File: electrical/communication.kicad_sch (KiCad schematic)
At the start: 23 parts

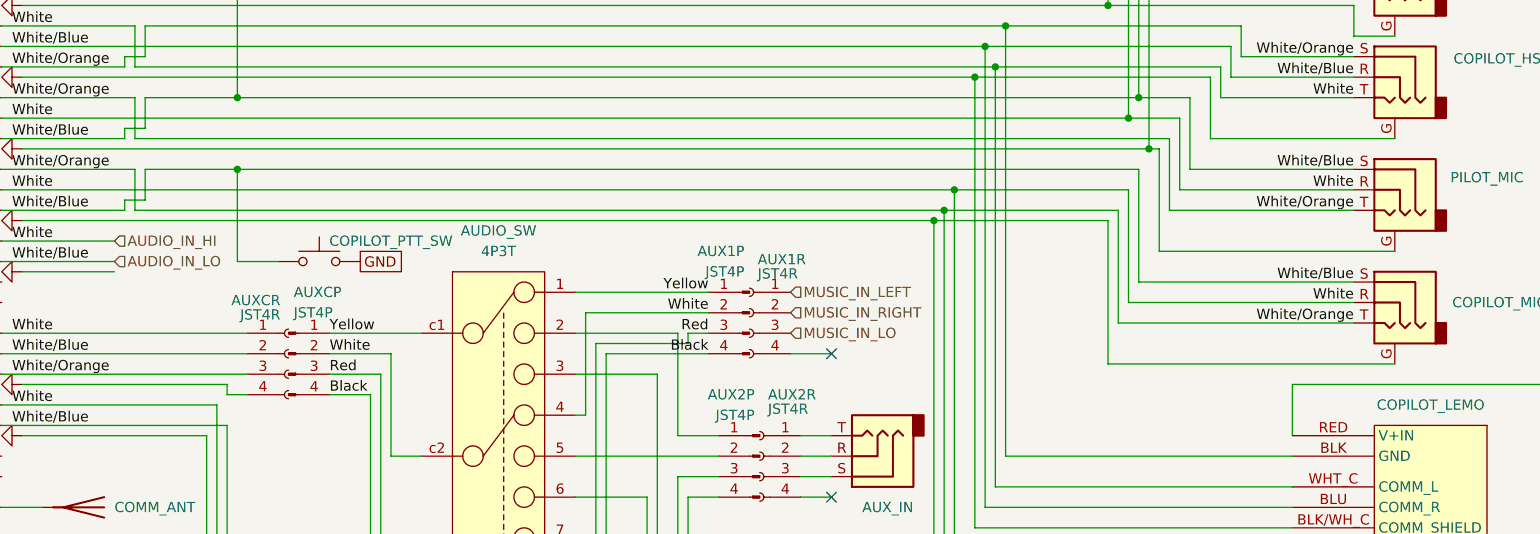
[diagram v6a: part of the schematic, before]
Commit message: Changed comms PTT and removed shield to TRS plugs. Fixed backwards GDU TX/RX wiring for GSU.
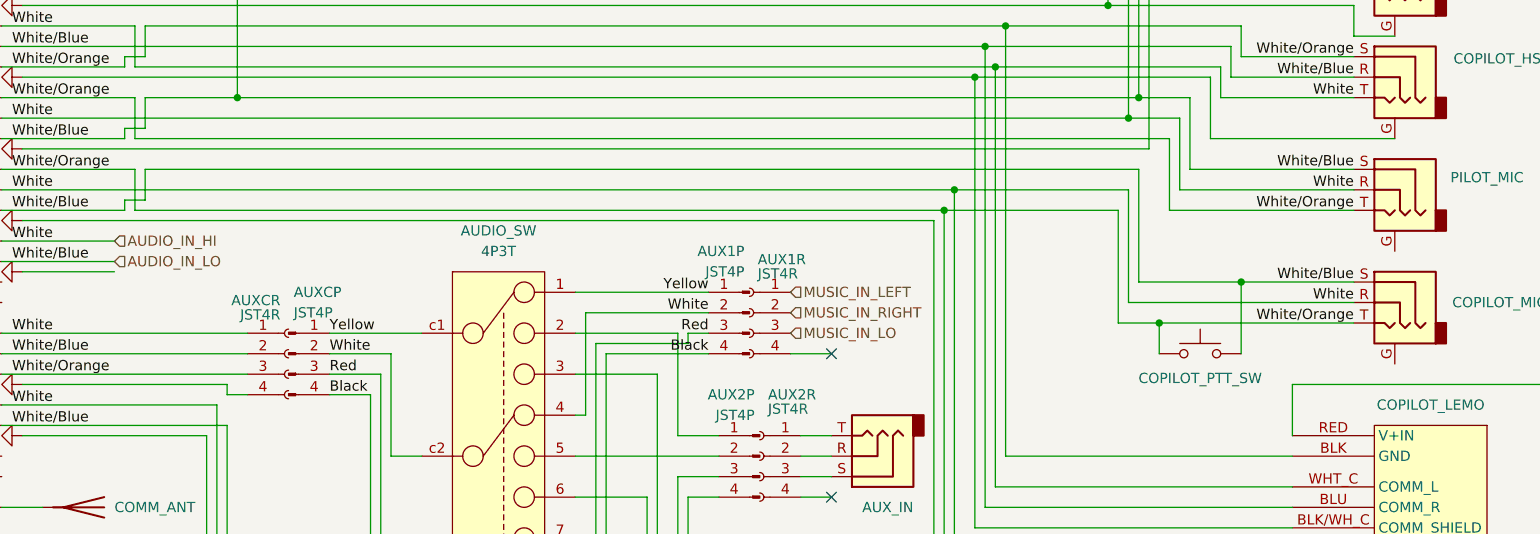
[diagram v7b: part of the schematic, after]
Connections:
- net AUDIO_IN_LO: now also COPILOT_PTT_SW.2; no longer COPILOT_PTT_SW.1
- net GND: no longer COPILOT_PTT_SW.2
- net GNDS: no longer COPILOT_MIC.G, PILOT_MIC.G
- net White/Orange: now also COPILOT_PTT_SW.1
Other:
- moved on the sheet: COPILOT_PTT_SW
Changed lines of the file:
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@@
 	(title_block
 		(title "Communication")
-		(date "2026-01-06")
-		(rev "1.2.5")
+		(date "2026-01-08")
+		(rev "1.2.6")
 		(company "N877RV")
 	)
@@
 	)
 	(junction
-		(at 180.34 87.63)
-		(diameter 0)
-		(color 0 0 0 0)
-	)
-	(junction
 		(at 76.2 34.29)
 		(diameter 0)
@@
 	)
 	(junction
-		(at 93.98 81.28)
-		(diameter 0)
-		(color 0 0 0 0)
-	)
-	(junction
 		(at 205.74 72.39)
 		(diameter 0)
@@
 	)
 	(junction
-		(at 198.12 54.61)
+		(at 208.28 100.33)
 		(diameter 0)
 		(color 0 0 0 0)
 	)
 	(junction
-		(at 207.01 78.74)
+		(at 198.12 54.61)
 		(diameter 0)
 		(color 0 0 0 0)
@@
 	)
 	(junction
+		(at 218.44 95.25)
+		(diameter 0)
+		(color 0 0 0 0)
+	)
+	(junction
 		(at 224.79 22.86)
 		(diameter 0)
@@
 	(wire
 		(pts
-			(xy 207.01 78.74) (xy 208.28 78.74)
-		)
-		(stroke
-			(width 0)
-			(type dash)
-		)
-	)
-	(wire
-		(pts
 			(xy 91.44 110.49) (xy 91.44 137.16)
 		)
@@
 	(wire
 		(pts
-			(xy 208.28 91.44) (xy 237.49 91.44)
-		)
-		(stroke
-			(width 0)
-			(type dash)
-		)
-	)
-	(wire
-		(pts
 			(xy 149.86 121.92) (xy 149.86 147.32)
 		)
@@
 	(wire
 		(pts
-			(xy 99.06 92.71) (xy 93.98 92.71)
-		)
-		(stroke
-			(width 0)
-			(type default)
-		)
-	)
-	(wire
-		(pts
 			(xy 81.28 63.5) (xy 81.28 68.58)
 		)
@@
 	(wire
 		(pts
-			(xy 201.93 105.41) (xy 237.49 105.41)
-		)
-		(stroke
-			(width 0)
-			(type dash)
-		)
-	)
-	(wire
-		(pts
 			(xy 224.79 107.95) (xy 256.54 107.95)
 		)
@@
 	(wire
 		(pts
-			(xy 180.34 87.63) (xy 201.93 87.63)
-		)
-		(stroke
-			(width 0)
-			(type dash)
-		)
-	)
-	(wire
-		(pts
 			(xy 232.41 59.69) (xy 199.39 59.69)
 		)
@@
 	(wire
 		(pts
+			(xy 218.44 95.25) (xy 205.74 95.25)
+		)
+		(stroke
+			(width 0)
+			(type default)
+		)
+	)
+	(wire
+		(pts
 			(xy 189.23 63.5) (xy 218.44 63.5)
 		)
@@
 	(wire
 		(pts
-			(xy 232.41 95.25) (xy 205.74 95.25)
+			(xy 232.41 95.25) (xy 218.44 95.25)
 		)
 		(stroke
@@
 	(wire
 		(pts
-			(xy 208.28 78.74) (xy 208.28 91.44)
-		)
-		(stroke
-			(width 0)
-			(type dash)
-		)
-	)
-	(wire
-		(pts
 			(xy 80.01 58.42) (xy 82.55 58.42)
 		)
@@
 	(wire
 		(pts
-			(xy 93.98 81.28) (xy 82.55 81.28)
+			(xy 82.55 81.28) (xy 205.74 81.28)
 		)
 		(stroke
@@
 	(wire
 		(pts
+			(xy 218.44 95.25) (xy 218.44 104.14)
+		)
+		(stroke
+			(width 0)
+			(type default)
+		)
+	)
+	(wire
+		(pts
 			(xy 213.36 22.86) (xy 224.79 22.86)
 		)
@@
 	(wire
 		(pts
-			(xy 201.93 87.63) (xy 201.93 105.41)
-		)
-		(stroke
-			(width 0)
-			(type dash)
-		)
-	)
-	(wire
-		(pts
 			(xy 201.93 60.96) (xy 201.93 34.29)
 		)
@@
 	(wire
 		(pts
-			(xy 93.98 92.71) (xy 93.98 81.28)
-		)
-		(stroke
-			(width 0)
-			(type default)
-		)
-	)
-	(wire
-		(pts
 			(xy 81.28 68.58) (xy 187.96 68.58)
 		)
@@
 	(wire
 		(pts
-			(xy 93.98 81.28) (xy 205.74 81.28)
-		)
-		(stroke
-			(width 0)
-			(type default)
-		)
-	)
-	(wire
-		(pts
 			(xy 212.09 81.28) (xy 232.41 81.28)
 		)
@@
 	(wire
 		(pts
+			(xy 208.28 100.33) (xy 232.41 100.33)
+		)
+		(stroke
+			(width 0)
+			(type default)
+		)
+	)
+	(wire
+		(pts
 			(xy 198.12 54.61) (xy 198.12 25.4)
 		)
@@
 	(wire
 		(pts
+			(xy 208.28 100.33) (xy 208.28 104.14)
+		)
+		(stroke
+			(width 0)
+			(type default)
+		)
+	)
+	(wire
+		(pts
 			(xy 256.54 16.51) (xy 224.79 16.51)
 		)
@@
 	(wire
 		(pts
-			(xy 203.2 100.33) (xy 232.41 100.33)
+			(xy 203.2 100.33) (xy 208.28 100.33)
 		)
 		(stroke
@@
 	(global_label "GND"
 		(shape passive)
-		(at 109.22 92.71 0)
-		(fields_autoplaced yes)
-		(effects
-			(font
-				(size 1.27 1.27)
-			)
-			(justify left)
-		)
-		(property "Intersheetrefs" "${INTERSHEET_REFS}"
-			(at 114.9644 92.71 0)
-			(effects
-				(font
-					(size 1.27 1.27)
-				)
-				(justify left)
-				(hide yes)
-			)
-		)
-	)
-	(global_label "GND"
-		(shape passive)
 		(at 45.72 137.16 0)
 		(fields_autoplaced yes)
@@
 	(symbol
 		(lib_id "Switch:SW_Push")
-		(at 104.14 92.71 0)
+		(at 213.36 104.14 0)
 		(unit 1)
 		(exclude_from_sim no)
@@
 		(dnp no)
 		(property "Reference" "COPILOT_PTT_SW"
-			(at 113.03 90.17 0)
+			(at 213.36 107.188 0)
 			(effects
 				(font
@@
 		)
 		(property "Value" "SW_Push"
-			(at 104.14 87.63 0)
+			(at 213.36 99.06 0)
 			(effects
 				(font
@@
 		)
 		(property "Footprint" ""
-			(at 104.14 87.63 0)
+			(at 213.36 99.06 0)
 			(effects
 				(font
@@
 		)
 		(property "Datasheet" "~"
-			(at 104.14 87.63 0)
+			(at 213.36 99.06 0)
 			(effects
 				(font
@@
 		)
 		(property "Description" ""
-			(at 104.14 92.71 0)
+			(at 213.36 104.14 0)
 			(effects
 				(font

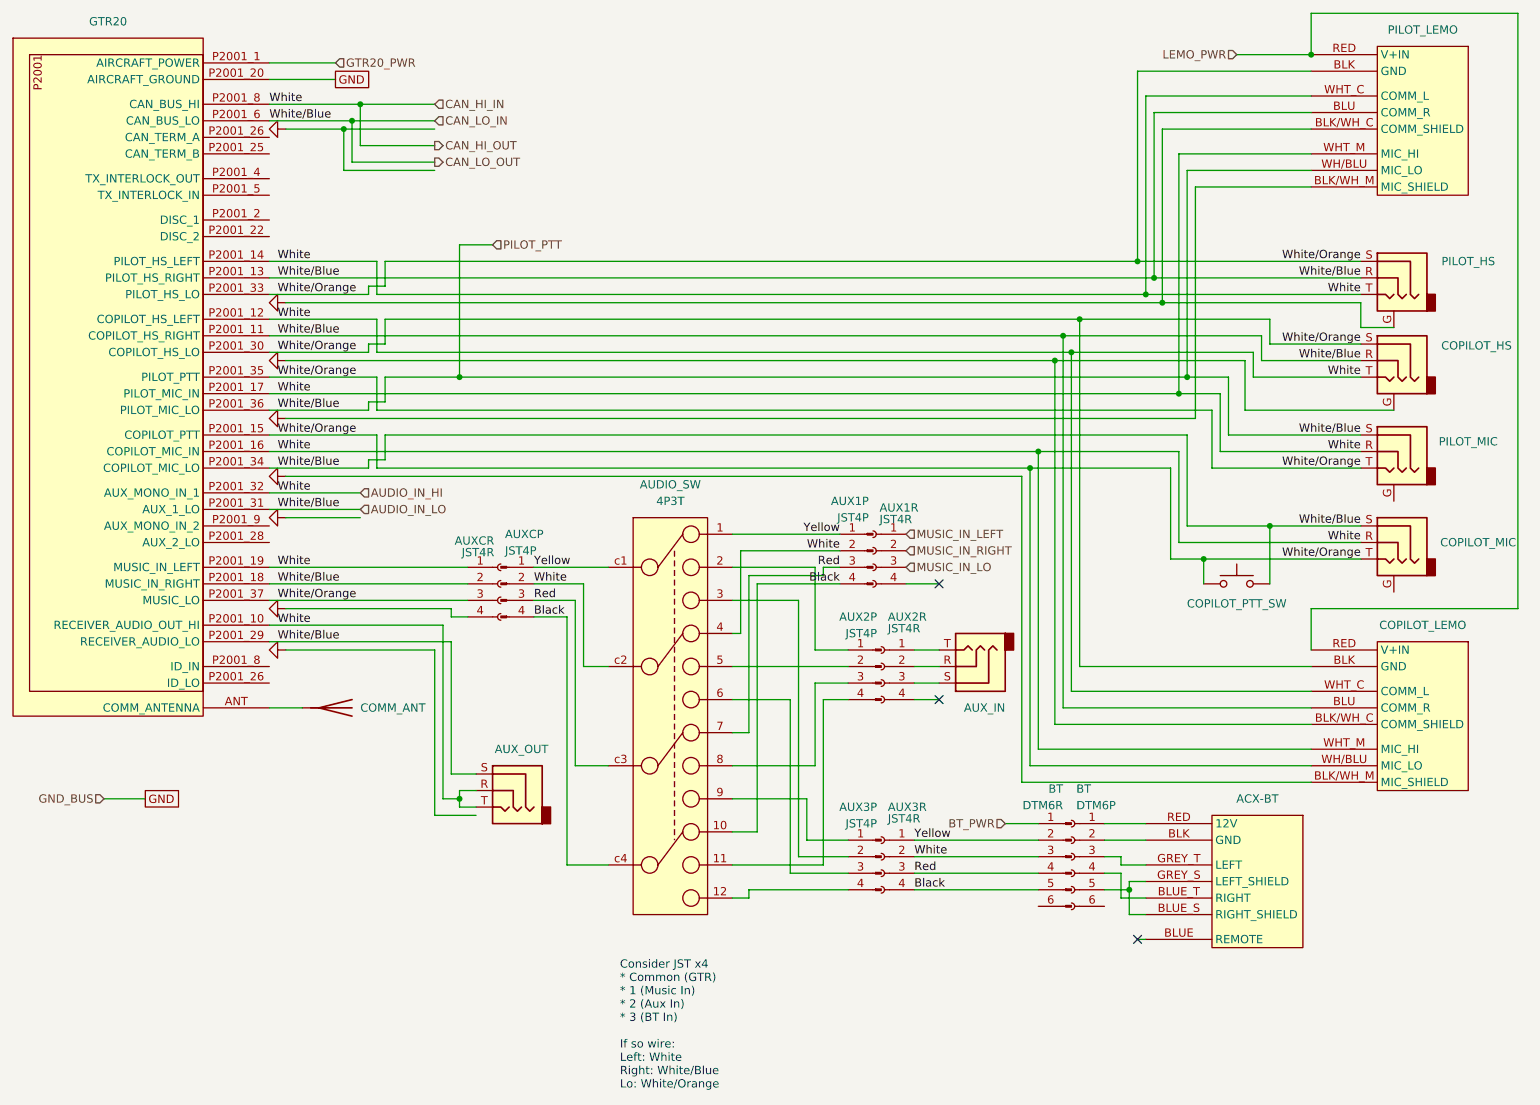
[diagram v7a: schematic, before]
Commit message: Cleaned up communications wiring for headphones and mic
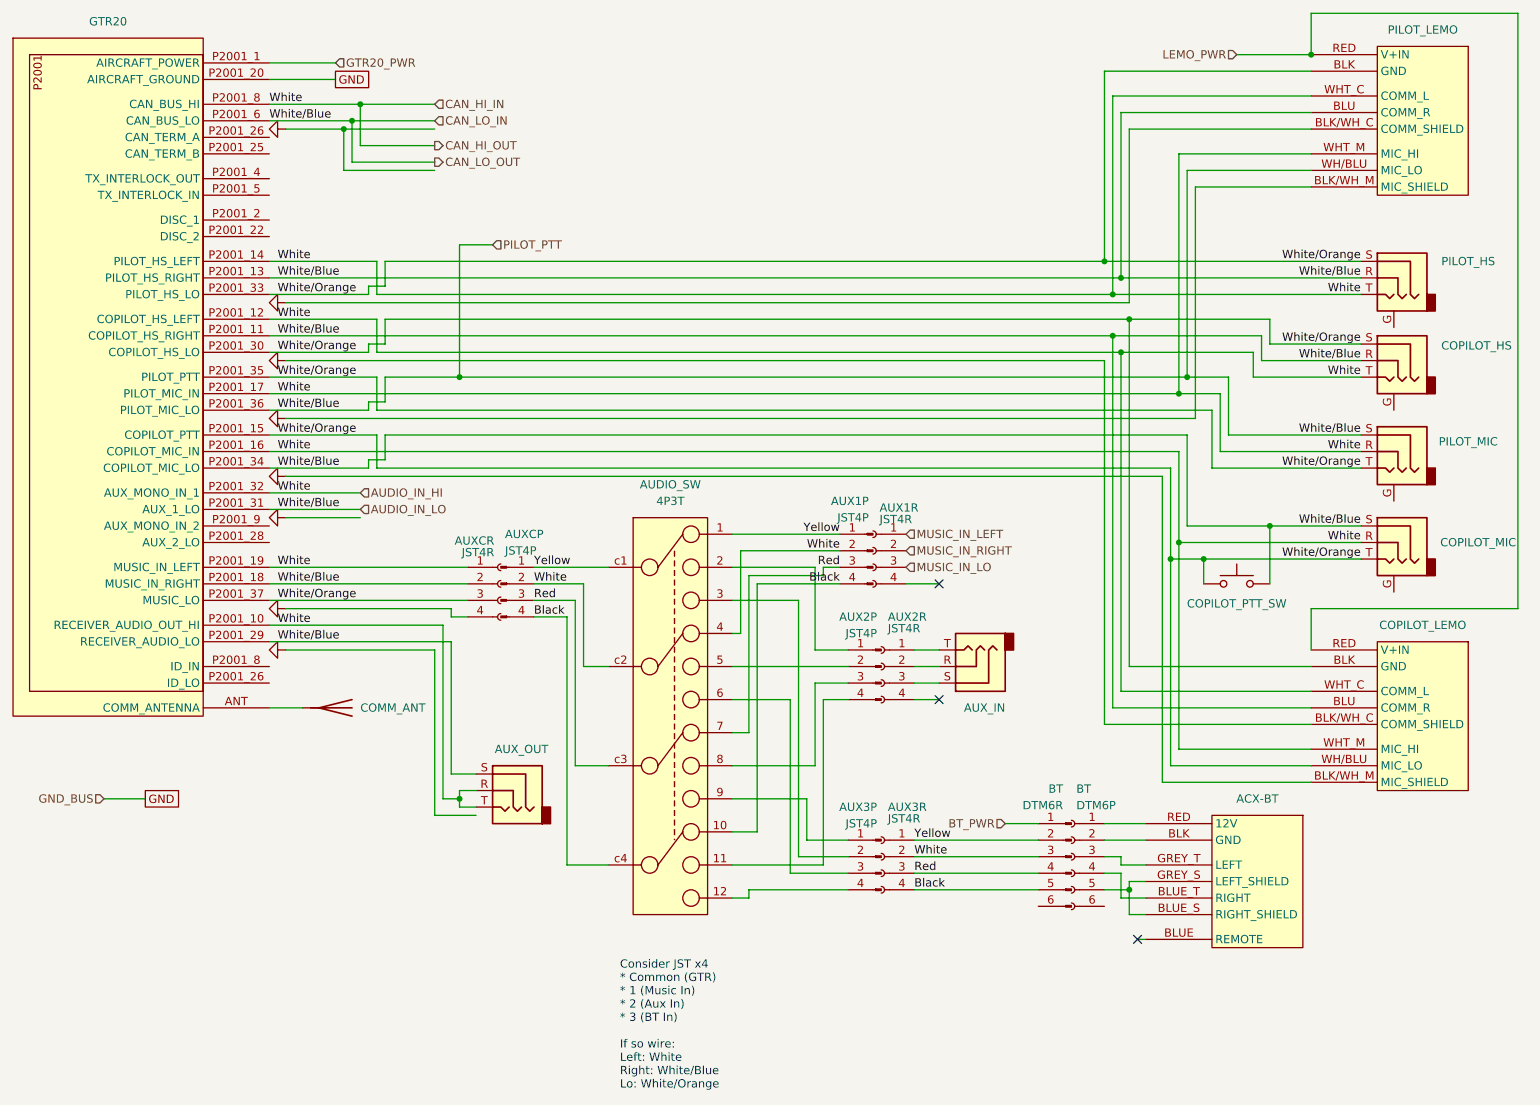
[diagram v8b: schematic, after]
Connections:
- net GNDS: no longer COPILOT_HS.G, PILOT_HS.G
